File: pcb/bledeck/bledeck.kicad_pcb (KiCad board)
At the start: 2 copper layers, 83 x 120 mm, 34 parts, among them J1 Conn_01x09_Socket, U1 ESP32-DEVKIT-V1

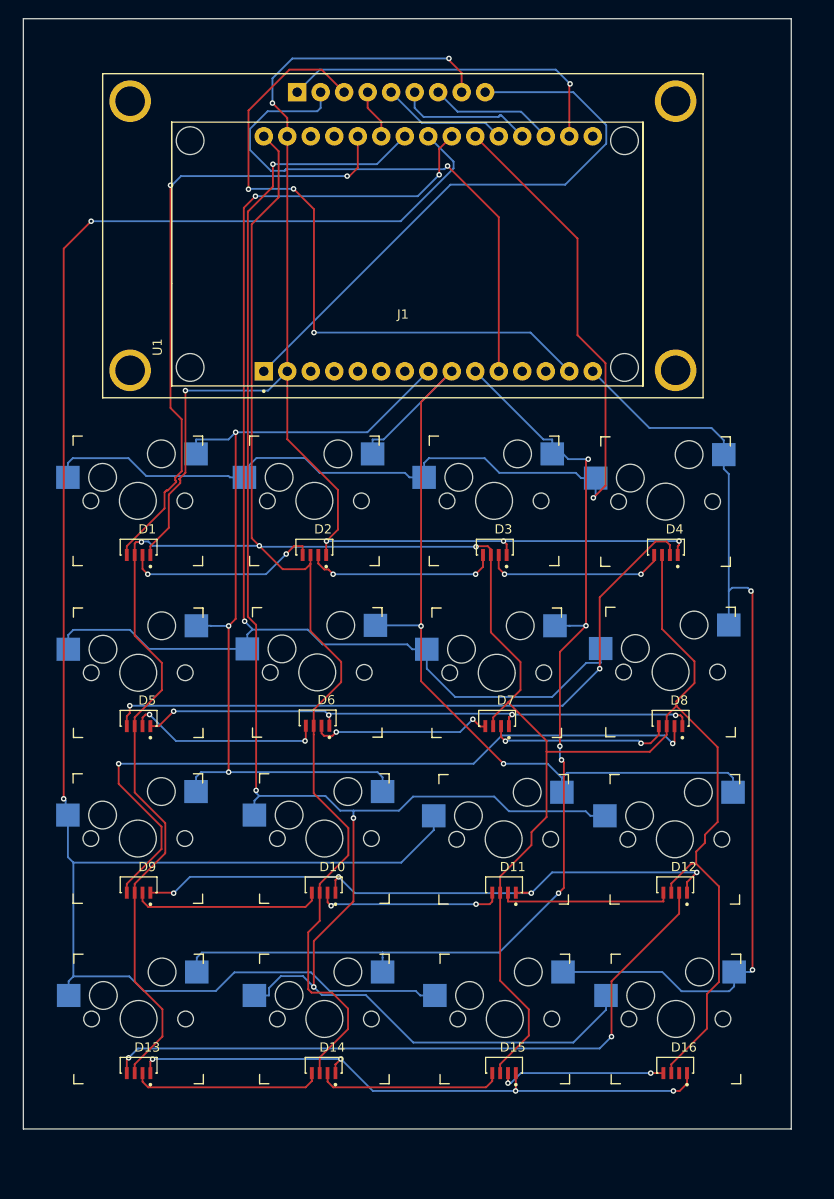
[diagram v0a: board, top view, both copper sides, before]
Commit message: generate gerber, fix pin number
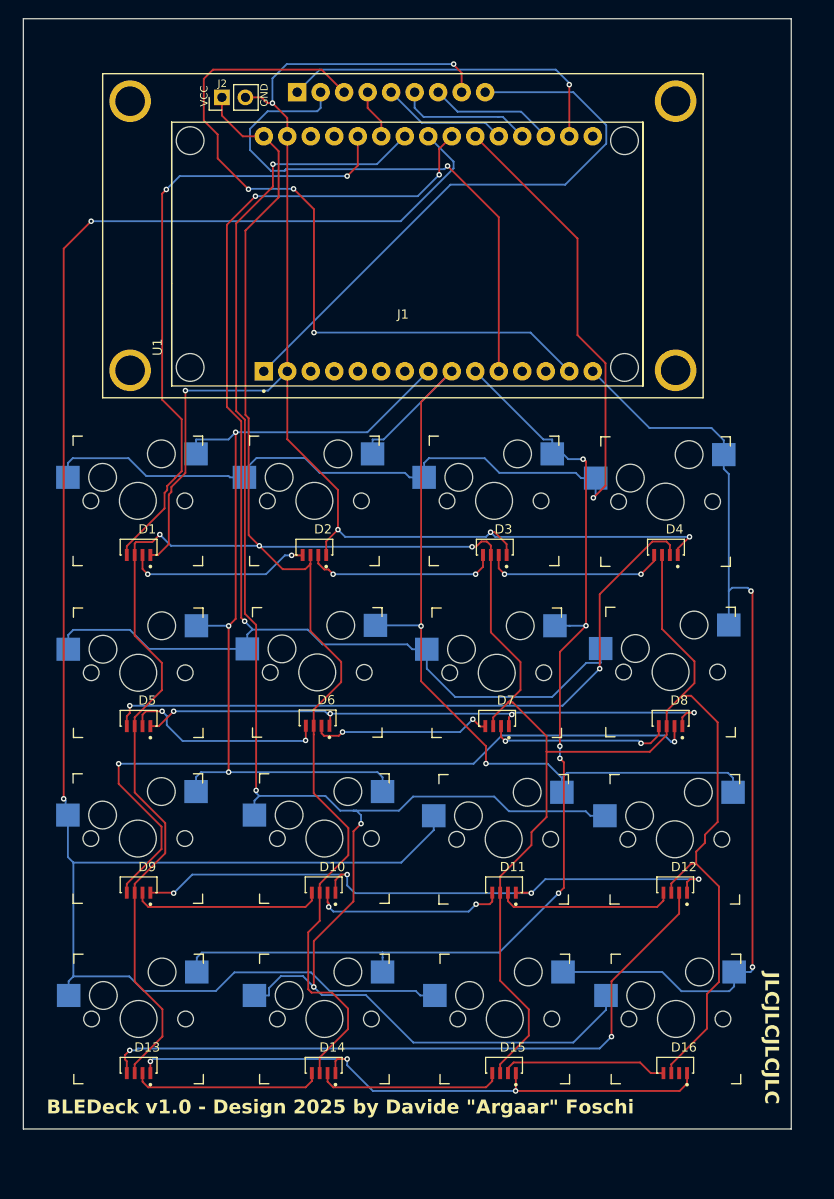
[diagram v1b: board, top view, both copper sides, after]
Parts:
- added J2: Conn_01x02_Socket, Connector_PinHeader_2.54mm:PinHeader_1x02_P2.54mm_Vertical, F.Cu at (101.5, 57.5)
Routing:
- net Net-(D1-VDD): track 377.7 -> 388.7 mm
- net Net-(J1-Pin_3): track 72.4 -> 81.2 mm
- net Net-(D1-VSS): track 151.8 -> 158.1 mm
- net Net-(D5-VSS): track 62.1 -> 64.9 mm
- net Net-(U1-D26): track 193.4 -> 195.3 mm
- net Net-(D10-VSS): track 67.6 -> 69.4 mm
- net Net-(U1-D33): track 142.5 -> 144.1 mm
- net Net-(D1-DOUT): track 21.3 -> 19.9 mm
- net Net-(D13-VSS): track 66.0 -> 67.3 mm, vias 4 -> 3
- net Net-(U1-D18): track 94.6 -> 95.7 mm
- net Net-(D5-DOUT): track 21.5 -> 22.5 mm
- net Net-(D10-DOUT): track 20.1 -> 20.9 mm
- net Net-(D12-DOUT): track 73.5 -> 74.0 mm
- net Net-(D15-DOUT): track 18.3 -> 18.1 mm, vias 2 -> 0
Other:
- board text added: "BLEDeck v1.0 - Design 2025 by Davide {dblquote}Argaar{dblquote} Foschi"
- board text added: "GND"
- board text added: "JLCJLCJLCJLC"
- board text added: "VCC"

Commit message: pcb add libraries and readme with licenses
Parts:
- J1: value Conn_01x09_Socket -> oled
- J2: footprint Connector_PinHeader_2.54mm:PinHeader_1x02_P2.54mm_Vertical -> BLEDeck:PinHeader_1x02_P2.54mm_Vertical
- S1, S10, S11, S12, S13, S14, S15, S16, S2, S3, S4, S5, S6, S7, S8, S9: footprint Connector:Kailh_socket_MX -> BLEDeck:Kailh_socket_MX
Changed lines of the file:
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@@
 	(net 47 "unconnected-(U1-RX0-Pad12)")
 	(net 48 "unconnected-(U1-D13-Pad28)")
-	(footprint "Connector:Kailh_socket_MX"
+	(footprint "BLEDeck:Kailh_socket_MX"
 		(layer "F.Cu")
 		(at 150.535 157.11)
@@
 		)
 	)
-	(footprint "Connector:Kailh_socket_MX"
+	(footprint "BLEDeck:Kailh_socket_MX"
 		(layer "F.Cu")
 		(at 112.535 157.11)
@@
 		)
 	)
-	(footprint "Connector:Kailh_socket_MX"
+	(footprint "BLEDeck:Kailh_socket_MX"
 		(layer "F.Cu")
 		(at 112.535 137.61)
@@
 		)
 	)
-	(footprint "Connector:Kailh_socket_MX"
+	(footprint "BLEDeck:Kailh_socket_MX"
 		(layer "F.Cu")
 		(at 149.415 101.19)
@@
 			)
 		)
-		(property "Value" "Conn_01x09_Socket"
+		(property "Value" "oled"
 			(at 0 8.5 0)
 			(layer "F.Fab")
@@
 			)
 		)
-		(property "Description" "Generic connector, single row, 01x09, script generated"
+		(property "Description" ""
 			(at 0 0 0)
 			(layer "F.Fab")
@@
 		)
 	)
-	(footprint "Connector:Kailh_socket_MX"
+	(footprint "BLEDeck:Kailh_socket_MX"
 		(layer "F.Cu")
 		(at 132.035 157.11)
@@
 		)
 	)
-	(footprint "Connector:Kailh_socket_MX"
+	(footprint "BLEDeck:Kailh_socket_MX"
 		(layer "F.Cu")
 		(at 150.415 137.69)
@@
 		)
 	)
-	(footprint "Connector:Kailh_socket_MX"
+	(footprint "BLEDeck:Kailh_socket_MX"
 		(layer "F.Cu")
 		(at 131.165 119.69)
@@
 		)
 	)
-	(footprint "Connector:Kailh_socket_MX"
+	(footprint "BLEDeck:Kailh_socket_MX"
 		(layer "F.Cu")
 		(at 131.915 137.69)
@@
 		)
 	)
-	(footprint "Connector:Kailh_socket_MX"
+	(footprint "BLEDeck:Kailh_socket_MX"
 		(layer "F.Cu")
 		(at 149.955 119.61)
@@
 		)
 	)
-	(footprint "Connector_PinHeader_2.54mm:PinHeader_1x02_P2.54mm_Vertical"
+	(footprint "BLEDeck:PinHeader_1x02_P2.54mm_Vertical"
 		(layer "F.Cu")
 		(at 101.46 57.5 90)
@@
 		(embedded_fonts no)
 	)
-	(footprint "Connector:Kailh_socket_MX"
+	(footprint "BLEDeck:Kailh_socket_MX"
 		(layer "F.Cu")
 		(at 111.765 119.65)
@@
 		)
 	)
-	(footprint "Connector:Kailh_socket_MX"
+	(footprint "BLEDeck:Kailh_socket_MX"
 		(layer "F.Cu")
 		(at 92.375 137.61)
@@
 		)
 	)
-	(footprint "Connector:Kailh_socket_MX"
+	(footprint "BLEDeck:Kailh_socket_MX"
 		(layer "F.Cu")
 		(at 111.455 101.11)
@@
 		)
 	)
-	(footprint "Connector:Kailh_socket_MX"
+	(footprint "BLEDeck:Kailh_socket_MX"
 		(layer "F.Cu")
 		(at 92.455 157.11)
@@
 		)
 	)
-	(footprint "Connector:Kailh_socket_MX"
+	(footprint "BLEDeck:Kailh_socket_MX"
 		(layer "F.Cu")
 		(at 92.415 119.69)
@@
 		)
 	)
-	(footprint "Connector:Kailh_socket_MX"
+	(footprint "BLEDeck:Kailh_socket_MX"
 		(layer "F.Cu")
 		(at 92.375 101.11)
@@
 		)
 	)
-	(footprint "Connector:Kailh_socket_MX"
+	(footprint "BLEDeck:Kailh_socket_MX"
 		(layer "F.Cu")
 		(at 130.875 101.11)

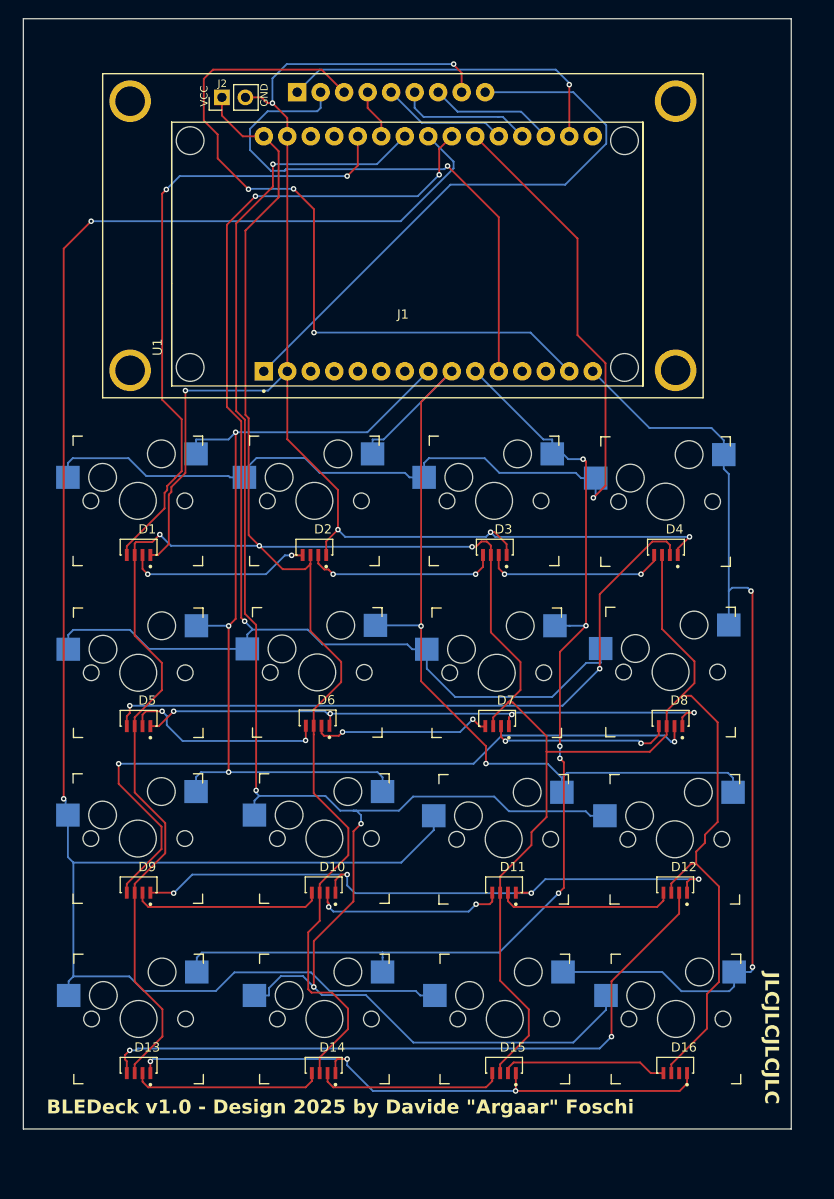
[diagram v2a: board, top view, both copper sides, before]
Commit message: [firmware] add battery info [pcb] evenly spaced keys, fix oled pins position, reroute all tracks/vias, add gerber zip for jlcpcb
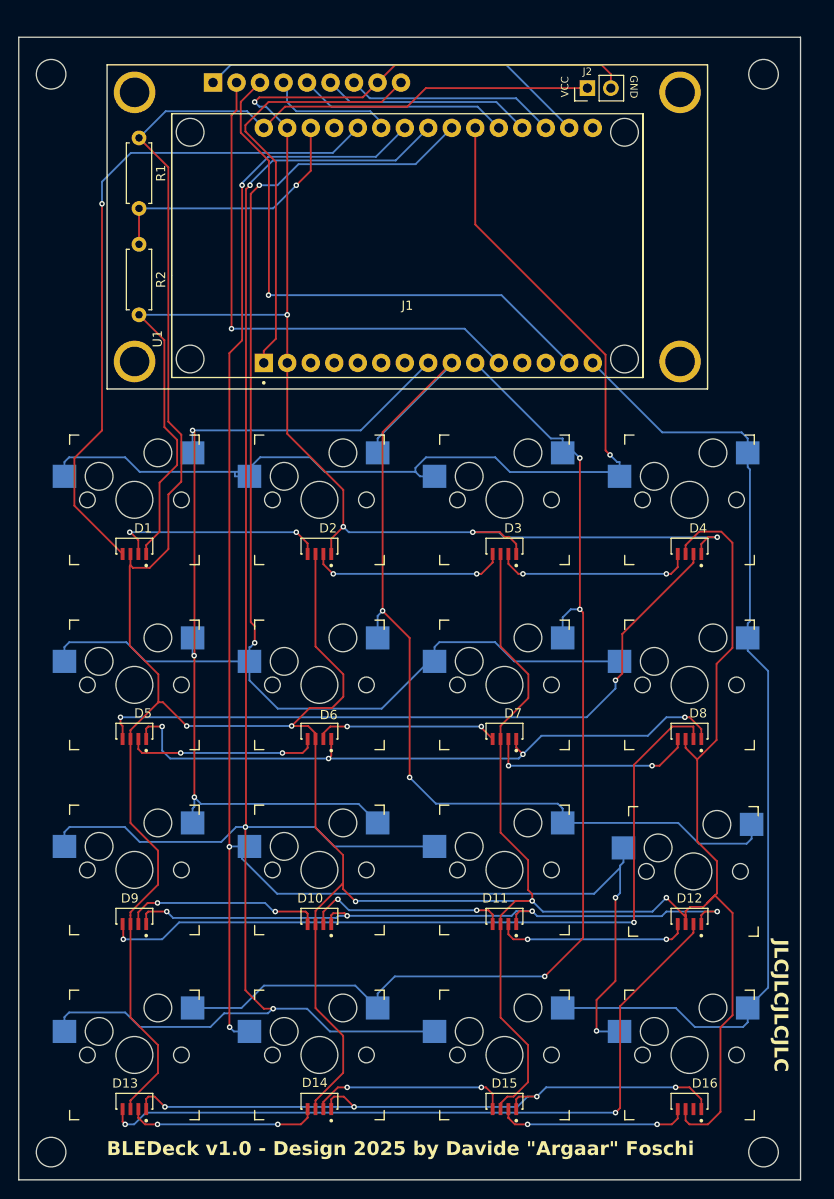
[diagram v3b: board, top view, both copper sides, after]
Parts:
- added R1: 15k, Resistor_THT:R_Axial_DIN0207_L6.3mm_D2.5mm_P7.62mm_Horizontal, F.Cu at (92.5, 61.9)
- added R2: 4.3k, Resistor_THT:R_Axial_DIN0207_L6.3mm_D2.5mm_P7.62mm_Horizontal, F.Cu at (92.5, 73.4)
- J1: value oled -> Conn_01x09_Socket
- moved J2 39.5 mm to (141.0, 56.5)
- moved D16 4.19 mm to (152.0, 166.0)
- moved S16 4.16 mm to (152.0, 161.0)
- moved S12 4.01 mm to (152.4, 141.2)
- moved S14 3.93 mm to (112.0, 161.0)
- moved D13 3.92 mm to (92.0, 166.0)
- moved D14 3.92 mm to (112.0, 166.0)
- moved S13 3.92 mm to (92.0, 161.0)
- moved D15 3.89 mm to (132.0, 166.0)
- moved S15 3.89 mm to (132.0, 161.0)
- moved D12 3.73 mm to (152.0, 146.0)
- moved S10 3.43 mm to (112.0, 141.0)
- moved D10 3.42 mm to (112.0, 146.0)
- moved D9 3.42 mm to (92.0, 146.0)
- moved S9 3.41 mm to (92.0, 141.0)
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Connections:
- U1 pad 28: unconnected-(U1-D13-Pad28) -> Net-(U1-D13)
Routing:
- net Net-(D1-VDD): track 388.7 -> 456.2 mm, vias 3 -> 5
- net Net-(D1-VSS): track 158.1 -> 191.4 mm, vias 6 -> 5
- net Net-(U1-D13): track 0.00 -> 28.8 mm, vias 0 -> 1
- net Net-(J1-Pin_3): track 81.2 -> 60.7 mm, vias 3 -> 1
- net Net-(J1-Pin_9): track 63.8 -> 46.3 mm
- net Net-(U1-D25): track 215.2 -> 201.2 mm, vias 2 -> 3
- net Net-(U1-D18): track 95.7 -> 107.9 mm
- net Net-(U1-D26): track 195.3 -> 185.8 mm, vias 4 -> 5
- net Net-(J1-Pin_7): track 13.6 -> 22.8 mm
- net Net-(J1-Pin_5): track 13.6 -> 22.8 mm
- net Net-(J1-Pin_4): track 5.38 -> 14.0 mm
- net Net-(J1-Pin_6): track 14.6 -> 22.8 mm
- net Net-(D5-VSS): track 64.9 -> 71.8 mm
- net Net-(U1-D19): track 114.6 -> 121.5 mm, vias 5 -> 3
- net Net-(D1-DIN): track 67.9 -> 73.7 mm, vias 2 -> 1
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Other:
- board size 83 x 120 mm -> 84.5 x 123.5 mm

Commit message: [firmware] add battery to display, fix oledupdate [pcb] fix keys connections, fix led traces, fix oled footprint [misc] add parts list to Readme
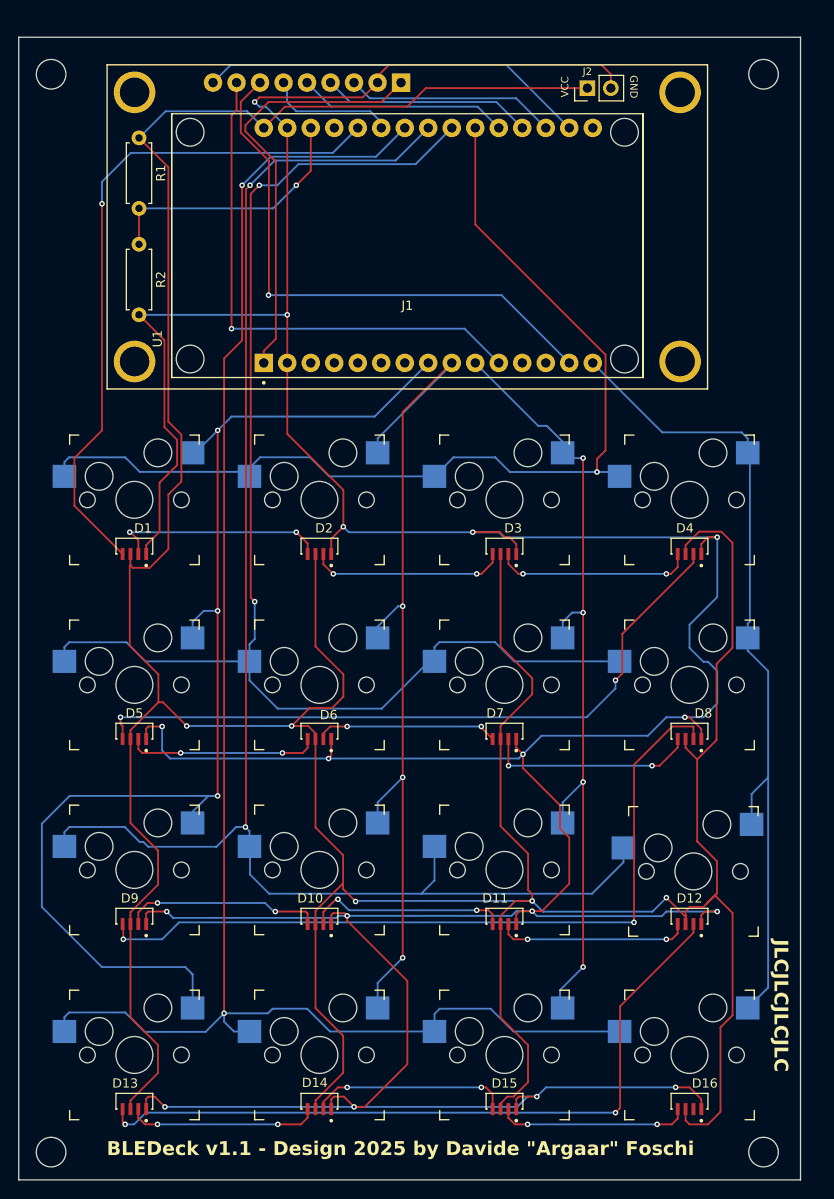
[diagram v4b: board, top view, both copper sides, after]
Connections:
- D10 pad 4: Net-(D10-VSS) -> Net-(D1-VSS)
- D11 pad 4: Net-(D10-VSS) -> Net-(D1-VSS)
- D12 pad 4: Net-(D10-VSS) -> Net-(D1-VSS)
- D13 pad 4: Net-(D13-VSS) -> Net-(D1-VSS)
- D14 pad 4: Net-(D13-VSS) -> Net-(D1-VSS)
- D15 pad 4: Net-(D13-VSS) -> Net-(D1-VSS)
- D16 pad 4: Net-(D13-VSS) -> Net-(D1-VSS)
- D5 pad 4: Net-(D5-VSS) -> Net-(D1-VSS)
- D6 pad 4: Net-(D5-VSS) -> Net-(D1-VSS)
- D7 pad 4: Net-(D5-VSS) -> Net-(D1-VSS)
- D8 pad 4: Net-(D5-VSS) -> Net-(D1-VSS)
- D9 pad 4: Net-(D10-VSS) -> Net-(D1-VSS)
- S10 pad 1: Net-(U1-D5) -> Net-(U1-D18)
- S10 pad 2: Net-(U1-D26) -> Net-(U1-D25)
- S11 pad 1: Net-(U1-D18) -> Net-(U1-D19)
- S12 pad 1: Net-(U1-D18) -> Net-(U1-D23)
- S12 pad 2: Net-(U1-D26) -> Net-(U1-D25)
- S13 pad 1: Net-(U1-D19) -> Net-(U1-D5)
- S13 pad 2: Net-(U1-D25) -> Net-(U1-D26)
- S14 pad 1: Net-(U1-D19) -> Net-(U1-D18)
- S15 pad 1: Net-(U1-D23) -> Net-(U1-D19)
- S15 pad 2: Net-(U1-D25) -> Net-(U1-D26)
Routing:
- net Net-(D1-VSS): track 191.4 -> 480.4 mm, vias 5 -> 17
- net Net-(D10-VSS): track 72.6 -> 0.00 mm, vias 4 -> 0
- net Net-(D5-VSS): track 71.8 -> 0.00 mm, vias 4 -> 0
- net Net-(D13-VSS): track 71.7 -> 0.00 mm, vias 4 -> 0
- net Net-(U1-D19): track 121.5 -> 86.5 mm, vias 3 -> 4
- net Net-(U1-D5): track 96.5 -> 130.3 mm
- net Net-(U1-D25): track 201.2 -> 169.7 mm, vias 3 -> 2
- net Net-(U1-D23): track 106.3 -> 90.0 mm
- net Net-(U1-D18): track 107.9 -> 97.0 mm, vias 2 -> 3
- net Net-(U1-D32): track 114.2 -> 108.2 mm
- net Net-(U1-D26): track 185.8 -> 182.4 mm, vias 5 -> 2
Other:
- board text added: "BLEDeck v1.1 - Design 2025 by Davide {dblquote}Argaar{dblquote} Foschi"
- board text removed: "BLEDeck v1.0 - Design 2025 by Davide {dblquote}Argaar{dblquote} Foschi"

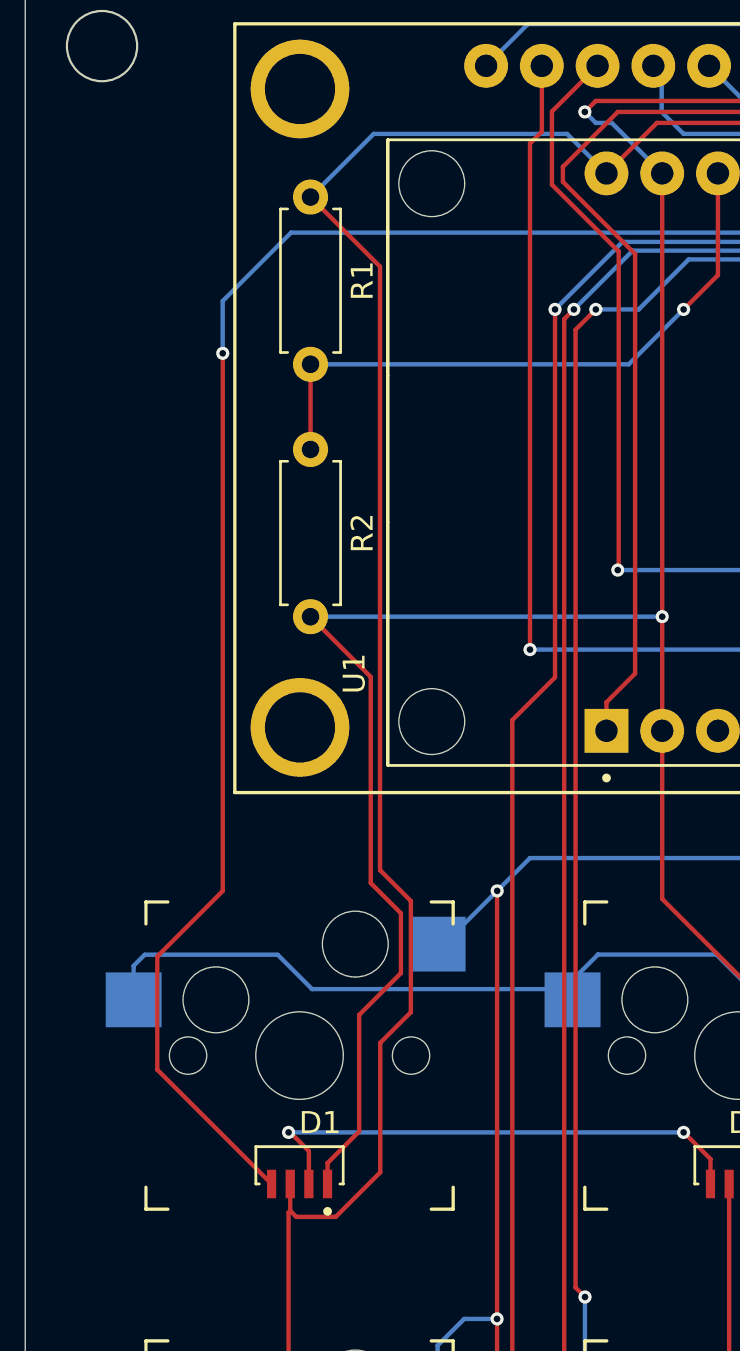
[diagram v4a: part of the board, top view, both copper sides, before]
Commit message: [pcb] version 1.1 [firmware] enabled 16 rgb, change keys layout
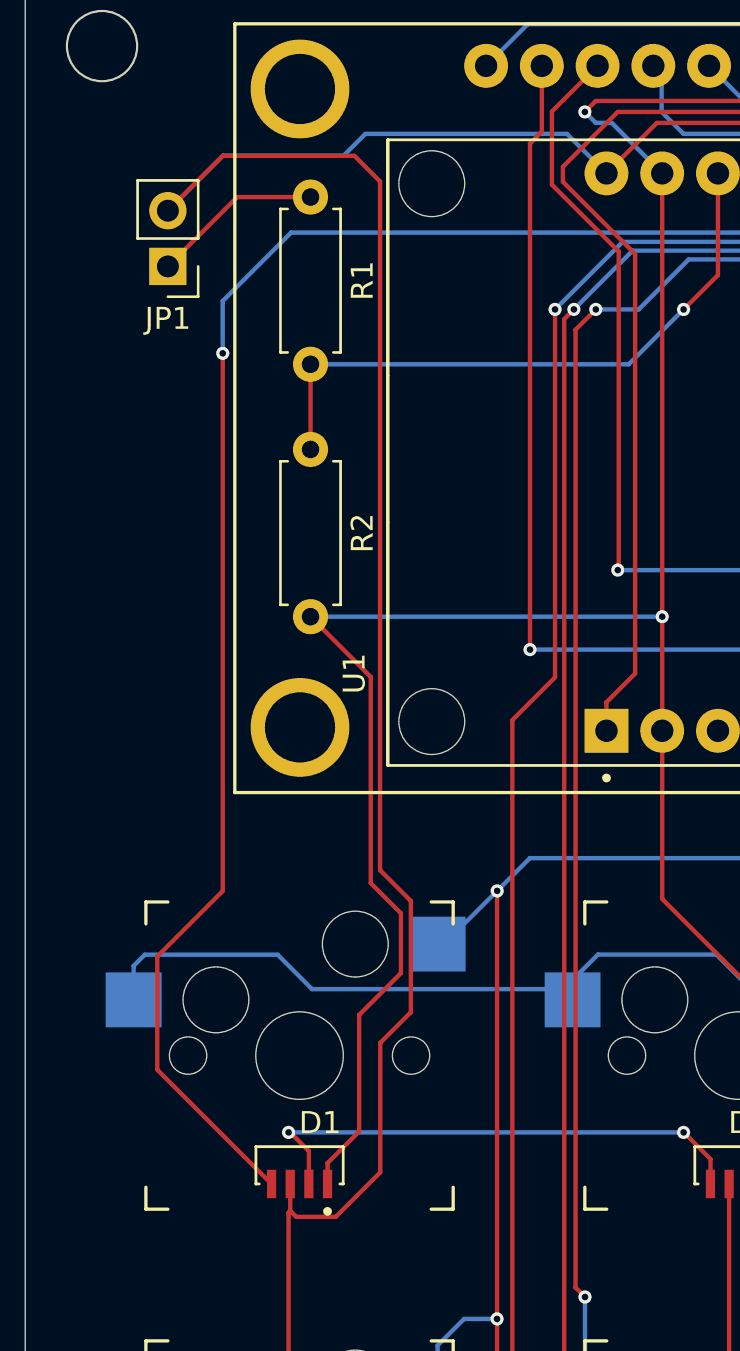
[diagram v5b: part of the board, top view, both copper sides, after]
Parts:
- added JP1: Jumper_Closed, BLEDeck:PinHeader_1x02_P2.54mm_Vertical, F.Cu at (86.0, 65.0)
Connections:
- R1 pad 1: Net-(D1-VDD) -> Net-(JP1-A)
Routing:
- net Net-(D1-VDD): track 456.6 -> 473.9 mm
- net Net-(JP1-A): track 0.00 -> 7.81 mm
